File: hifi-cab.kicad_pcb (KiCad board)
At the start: 2 copper layers, 25 parts, among them J1 FAN 1, J10 BUTTON, J11 RS-232, J12 5V ENABLE, J13 PWR IN, J2 FAN VOLTAGE, J3 FAN 1, J7 IR REMOTE, J8 DS18B20, J9 DS18B20, Q1 AO3400A, Q2 AO3400A, U1 esp32-wemos-d1-mini, U2 TSR1-2433E

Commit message: Update hifi-cab.kicad_pcb
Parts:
- added REF**: MountingHole_2.5mm_Pad_TopOnly, MountingHole:MountingHole_2.5mm_Pad_TopOnly, F.Cu at (44.7, 151.6)
- moved R11 106.8 mm to (70.0, 145.0)
- moved J10 103.6 mm to (66.5, 151.4)
- moved J11 98.2 mm to (52.3, 151.5)
- moved U1 45.0 mm to (104.3, 134.8), turned to 0 degrees
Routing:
- net +3.3V: track 2.45 -> 9.19 mm
- net BTN_1: track 0.00 -> 6.48 mm

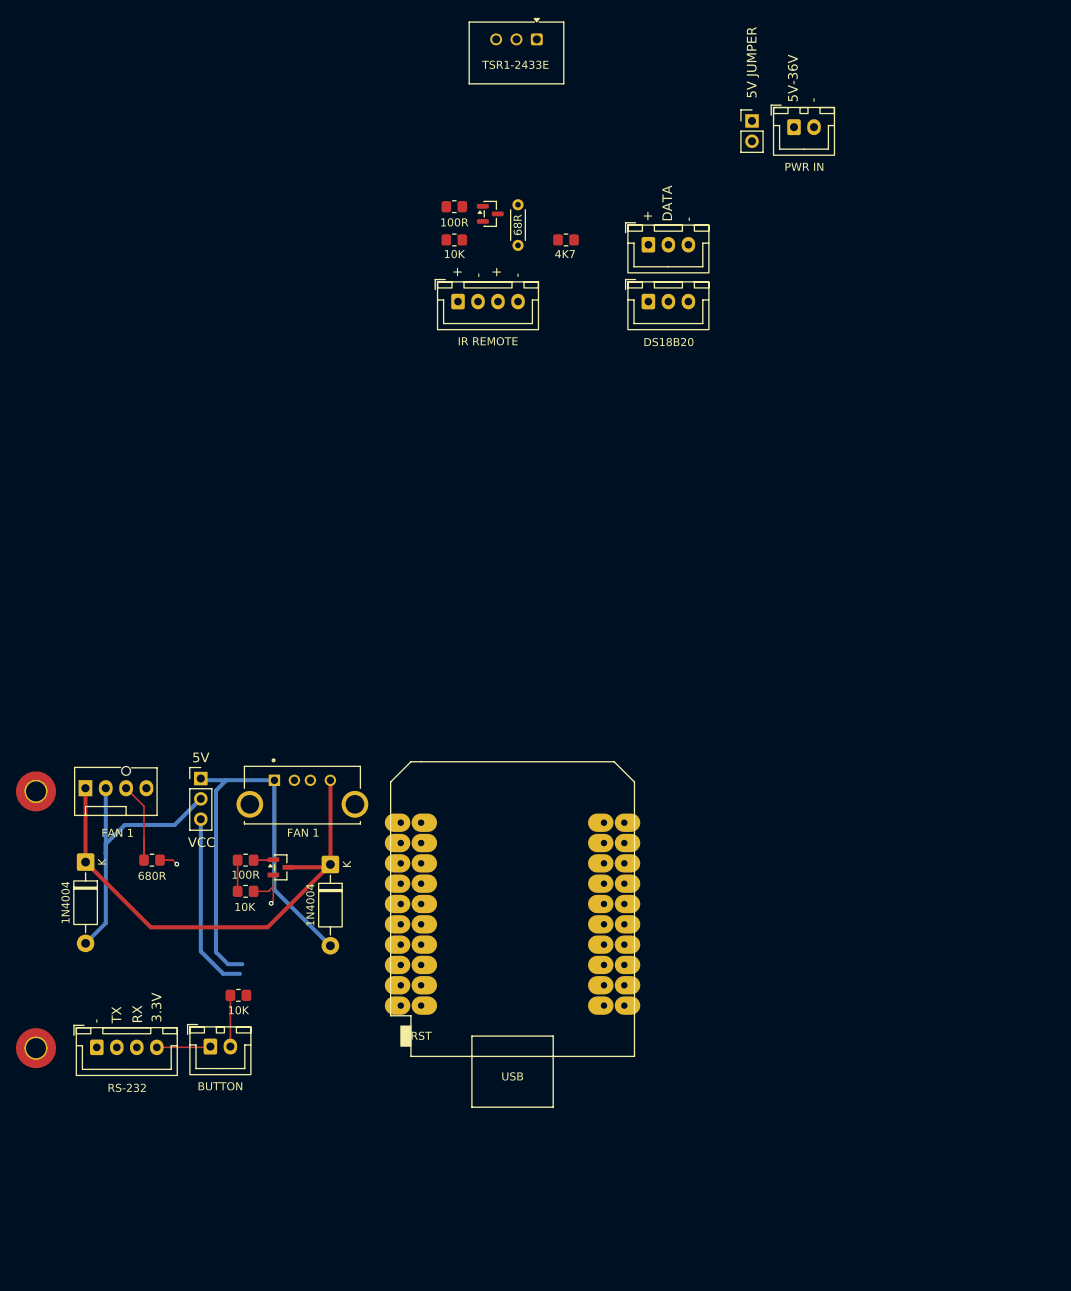
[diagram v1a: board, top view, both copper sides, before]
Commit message: Simplify, return to 5V only.
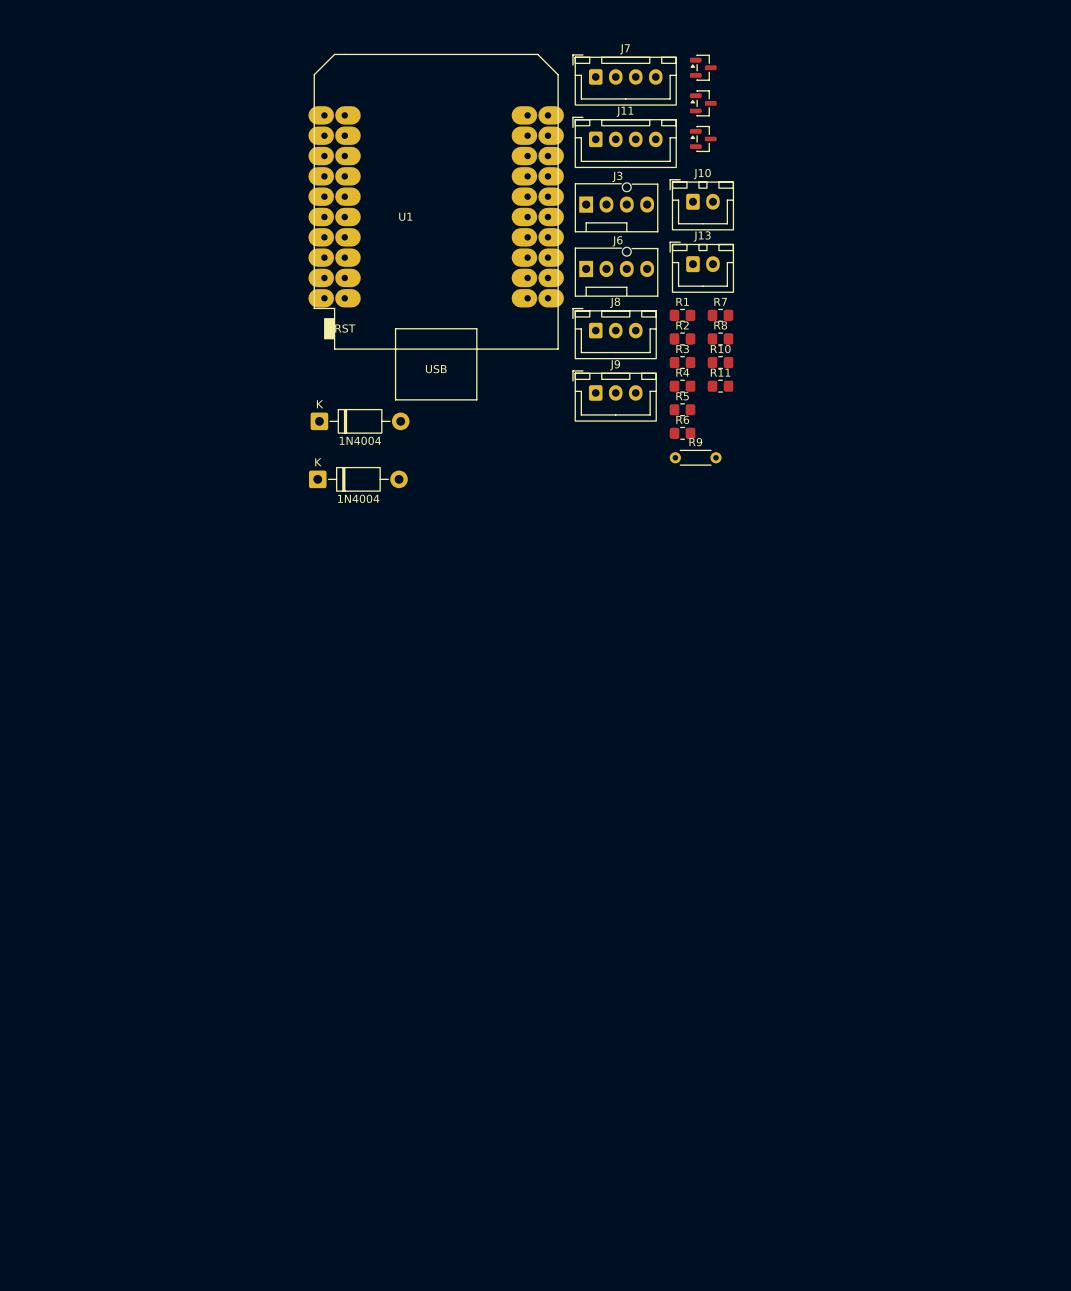
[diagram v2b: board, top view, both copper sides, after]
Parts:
- removed D1: 1N4004, Diode_THT:D_DO-41_SOD81_P10.16mm_Horizontal
- removed J1: FAN 1, USB_A1VSB6:ONSHORE_USB-A1VSB6
- removed J12: 5V ENABLE, Connector_PinHeader_2.54mm:PinHeader_1x02_P2.54mm_Vertical
- removed J2: FAN VOLTAGE, Connector_PinHeader_2.54mm:PinHeader_1x03_P2.54mm_Vertical
- removed REF** (x2): MountingHole_2.5mm_Pad_TopOnly, MountingHole:MountingHole_2.5mm_Pad_TopOnly
- removed U2: TSR1-2433E, Converter_DCDC:Converter_DCDC_TRACO_TSR1-xxxxE_THT
- added D4: 1N4004, Diode_THT:D_DO-41_SOD81_P10.16mm_Horizontal, F.Cu at (79.9, 80.5)
- added J6: FAN 2, Connector:FanPinHeader_1x04_P2.54mm_Vertical, F.Cu at (113.5, 54.2)
- added Q3: AO3400A, Package_TO_SOT_SMD:SOT-23, F.Cu at (128.1, 38.0)
- added R4: 100R, Resistor_SMD:R_0805_2012Metric_Pad1.20x1.40mm_HandSolder, F.Cu at (125.5, 68.8)
- added R5: 10K, Resistor_SMD:R_0805_2012Metric_Pad1.20x1.40mm_HandSolder, F.Cu at (125.5, 71.8)
- added R6: 680R, Resistor_SMD:R_0805_2012Metric_Pad1.20x1.40mm_HandSolder, F.Cu at (125.5, 74.8)
- moved J11 129.5 mm to (114.7, 38.0)
- moved J10 121.6 mm to (126.8, 45.8)
- moved Q1 113.0 mm to (128.1, 29.1)
- moved R11 97.1 mm to (130.3, 68.8)
- moved J3 96.1 mm to (113.5, 46.1)
- moved R3 90.9 mm to (125.5, 65.9)
- moved U1 88.9 mm to (94.7, 46.4)
- moved R2 88.0 mm to (125.5, 63.0)
- moved R1 87.3 mm to (125.5, 60.0)
- moved D2 62.4 mm to (80.1, 73.2), turned to 0 degrees
- moved R7 35.9 mm to (130.3, 60.0)
- moved R8 35.5 mm to (130.3, 63.0)
- moved R9 33.0 mm to (124.6, 77.8), turned to 0 degrees
- moved J7 32.9 mm to (114.7, 30.2)
- moved Q2 30.0 mm to (128.1, 33.5)
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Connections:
- J13 pad 1: VCC -> +5V
- U1 pad 35: unconnected-(U1-VCC_(USB)-Pad35) -> +5V
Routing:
- net FAN1: track 62.4 -> 0.00 mm
- net +5V: track 59.5 -> 0.00 mm
- net Net-(D2-A): track 35.9 -> 0.00 mm
- net VCC: track 22.6 -> 0.00 mm
- net TACH1: track 11.9 -> 0.00 mm
- net +3.3V: track 9.19 -> 0.00 mm, vias 1 -> 0
- net BTN_1: track 6.48 -> 0.00 mm
- net GND: track 6.37 -> 0.00 mm, vias 1 -> 0
- net FAN1_C: track 3.90 -> 0.00 mm
- net Net-(Q1-G): track 2.48 -> 0.00 mm
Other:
- board text removed: "+"
- board text removed: "-"
- board text removed: "3.3V"
- board text removed: "5V"
- board text removed: "5V JUMPER"
- board text removed: "5V-36V"
- board text removed: "DATA"
- board text removed: "RX"
- board text removed: "TX"
- board text removed: "VCC"

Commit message: Add cap
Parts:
- added C1: 400uF, Capacitor_THT:CP_Radial_D5.0mm_P2.50mm, F.Cu at (123.3, 59.2)
- moved Q1 80.3 mm to (110.7, 107.5), turned to 90 degrees
- moved Q3 69.6 mm to (125.7, 107.5), turned to 90 degrees
- moved R2 54.1 mm to (110.7, 115.0), turned to 180 degrees
- moved R1 53.5 mm to (110.7, 111.4), turned to 180 degrees
- moved J3 49.3 mm to (104.7, 94.7)
- moved R4 49.1 mm to (127.1, 118.0)
- moved R5 49.1 mm to (127.1, 120.9)
- moved D4 45.5 mm to (119.6, 102.7), turned to -90 degrees
- moved R9 43.6 mm to (136.6, 35.9)
- moved J6 41.0 mm to (119.6, 94.7)
- moved R3 39.3 mm to (110.8, 102.3)
- moved D2 38.4 mm to (104.7, 102.7), turned to -90 degrees
- moved R11 29.4 mm to (150.0, 47.1)
- moved J8 28.9 mm to (143.4, 65.0)
- moved J9 28.8 mm to (143.4, 71.9)
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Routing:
- net Net-(D4-A): track 0.00 -> 19.2 mm
- net Net-(D2-A): track 0.00 -> 19.2 mm
- net FAN1: track 0.00 -> 15.8 mm
- net FAN2: track 0.00 -> 15.7 mm
- net TACH1: track 0.00 -> 7.67 mm
- net TACH2: track 0.00 -> 7.62 mm
- net FAN1_C: track 0.00 -> 3.60 mm
- net Net-(Q1-G): track 0.00 -> 3.00 mm

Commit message: Update hifi-cab.kicad_pcb
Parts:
- moved R4 6.70 mm to (125.7, 111.4), turned to 180 degrees
- moved R5 6.06 mm to (125.7, 115.0), turned to 180 degrees
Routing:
- net GND: track 0.00 -> 9.89 mm, vias 0 -> 4
- net FAN2_C: track 0.00 -> 3.60 mm
- net Net-(Q3-G): track 0.00 -> 3.02 mm
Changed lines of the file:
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@@
 	(footprint "Resistor_SMD:R_0805_2012Metric_Pad1.20x1.40mm_HandSolder"
 		(layer "F.Cu")
-		(at 127.1 120.9)
+		(at 125.7 115 180)
 		(descr "Resistor SMD 0805 (2012 Metric), square (rectangular) end terminal, IPC-7351 nominal with elongated pad for handsoldering. (Body size source: IPC-SM-782 page 72, https://www.pcb-3d.com/wordpress/wp-content/uploads/ipc-sm-782a_amendment_1_and_2.pdf), generated with kicad-footprint-generator")
 		(tags "resistor handsolder")
@@
 		)
 		(property "Value" "10K"
-			(at 0 1.65 0)
+			(at 0 -1.8 0)
 			(layer "F.SilkS")
 			(effects
@@
 		(attr smd)
 		(fp_line
-			(start -0.227064 -0.735)
-			(end 0.227064 -0.735)
+			(start -0.227064 0.735)
+			(end 0.227064 0.735)
 			(stroke
 				(width 0.12)
@@
 		)
 		(fp_line
-			(start -0.227064 0.735)
-			(end 0.227064 0.735)
+			(start -0.227064 -0.735)
+			(end 0.227064 -0.735)
 			(stroke
 				(width 0.12)
@@
 		)
 		(pad "1" smd roundrect
-			(at -1 0)
+			(at -1 0 180)
 			(size 1.2 1.4)
 			(layers "F.Cu" "F.Mask" "F.Paste")
@@
 		)
 		(pad "2" smd roundrect
-			(at 1 0)
+			(at 1 0 180)
 			(size 1.2 1.4)
 			(layers "F.Cu" "F.Mask" "F.Paste")
@@
 	(footprint "Resistor_SMD:R_0805_2012Metric_Pad1.20x1.40mm_HandSolder"
 		(layer "F.Cu")
-		(at 127.1 117.95)
+		(at 125.7 111.4 180)
 		(descr "Resistor SMD 0805 (2012 Metric), square (rectangular) end terminal, IPC-7351 nominal with elongated pad for handsoldering. (Body size source: IPC-SM-782 page 72, https://www.pcb-3d.com/wordpress/wp-content/uploads/ipc-sm-782a_amendment_1_and_2.pdf), generated with kicad-footprint-generator")
 		(tags "resistor handsolder")
@@
 		)
 		(property "Value" "100R"
-			(at 0 1.65 0)
+			(at 0 -1.8 0)
 			(layer "F.SilkS")
 			(effects
@@
 		(attr smd)
 		(fp_line
-			(start -0.227064 -0.735)
-			(end 0.227064 -0.735)
+			(start -0.227064 0.735)
+			(end 0.227064 0.735)
 			(stroke
 				(width 0.12)
@@
 		)
 		(fp_line
-			(start -0.227064 0.735)
-			(end 0.227064 0.735)
+			(start -0.227064 -0.735)
+			(end 0.227064 -0.735)
 			(stroke
 				(width 0.12)
@@
 		)
 		(pad "1" smd roundrect
-			(at -1 0)
+			(at -1 0 180)
 			(size 1.2 1.4)
 			(layers "F.Cu" "F.Mask" "F.Paste")
@@
 		)
 		(pad "2" smd roundrect
-			(at 1 0)
+			(at 1 0 180)
 			(size 1.2 1.4)
 			(layers "F.Cu" "F.Mask" "F.Paste")
@@
 	)
 	(segment
+		(start 124.65 115.05)
+		(end 123.75 114.15)
+		(width 0.2)
+		(layer "F.Cu")
+		(net 11)
+	)
+	(segment
+		(start 111.6 108.4)
+		(end 112.5 109.3)
+		(width 0.2)
+		(layer "F.Cu")
+		(net 11)
+	)
+	(segment
+		(start 126.65 108.35)
+		(end 127.55 109.25)
+		(width 0.2)
+		(layer "F.Cu")
+		(net 11)
+	)
+	(segment
+		(start 127.55 109.25)
+		(end 128.75 109.25)
+		(width 0.2)
+		(layer "F.Cu")
+		(net 11)
+	)
+	(segment
+		(start 123.75 114.15)
+		(end 122.55 114.15)
+		(width 0.2)
+		(layer "F.Cu")
+		(net 11)
+	)
+	(segment
+		(start 109.65 115.15)
+		(end 108.75 114.25)
+		(width 0.2)
+		(layer "F.Cu")
+		(net 11)
+	)
+	(segment
+		(start 108.75 114.25)
+		(end 107.55 114.25)
+		(width 0.2)
+		(layer "F.Cu")
+		(net 11)
+	)
+	(segment
+		(start 112.5 109.3)
+		(end 113.7 109.3)
+		(width 0.2)
+		(layer "F.Cu")
+		(net 11)
+	)
+	(via
+		(at 128.75 109.25)
+		(size 0.6)
+		(drill 0.3)
+		(layers "F.Cu" "B.Cu")
+		(net 11)
+	)
+	(via
+		(at 107.55 114.25)
+		(size 0.6)
+		(drill 0.3)
+		(layers "F.Cu" "B.Cu")
+		(net 11)
+	)
+	(via
+		(at 122.55 114.15)
+		(size 0.6)
+		(drill 0.3)
+		(layers "F.Cu" "B.Cu")
+		(net 11)
+	)
+	(via
+		(at 113.7 109.3)
+		(size 0.6)
+		(drill 0.3)
+		(layers "F.Cu" "B.Cu")
+		(net 11)
+	)
+	(segment
 		(start 109.7 108.4)
 		(end 109.7 111.4)
@@
 	)
 	(segment
+		(start 126.7 111.4)
+		(end 126.7 115)
+		(width 0.2)
+		(layer "F.Cu")
+		(net 20)
+	)
+	(segment
 		(start 125.7 106.525)
 		(end 121.895 102.72)
@@
 		(net 46)
 	)
+	(segment
+		(start 124.75 111.35)
+		(end 124.7 111.4)
+		(width 0.2)
+		(layer "F.Cu")
+		(net 47)
+	)
+	(segment
+		(start 124.75 108.4)
+		(end 124.75 111.35)
+		(width 0.2)
+		(layer "F.Cu")
+		(net 47)
+	)
 	(embedded_fonts no)

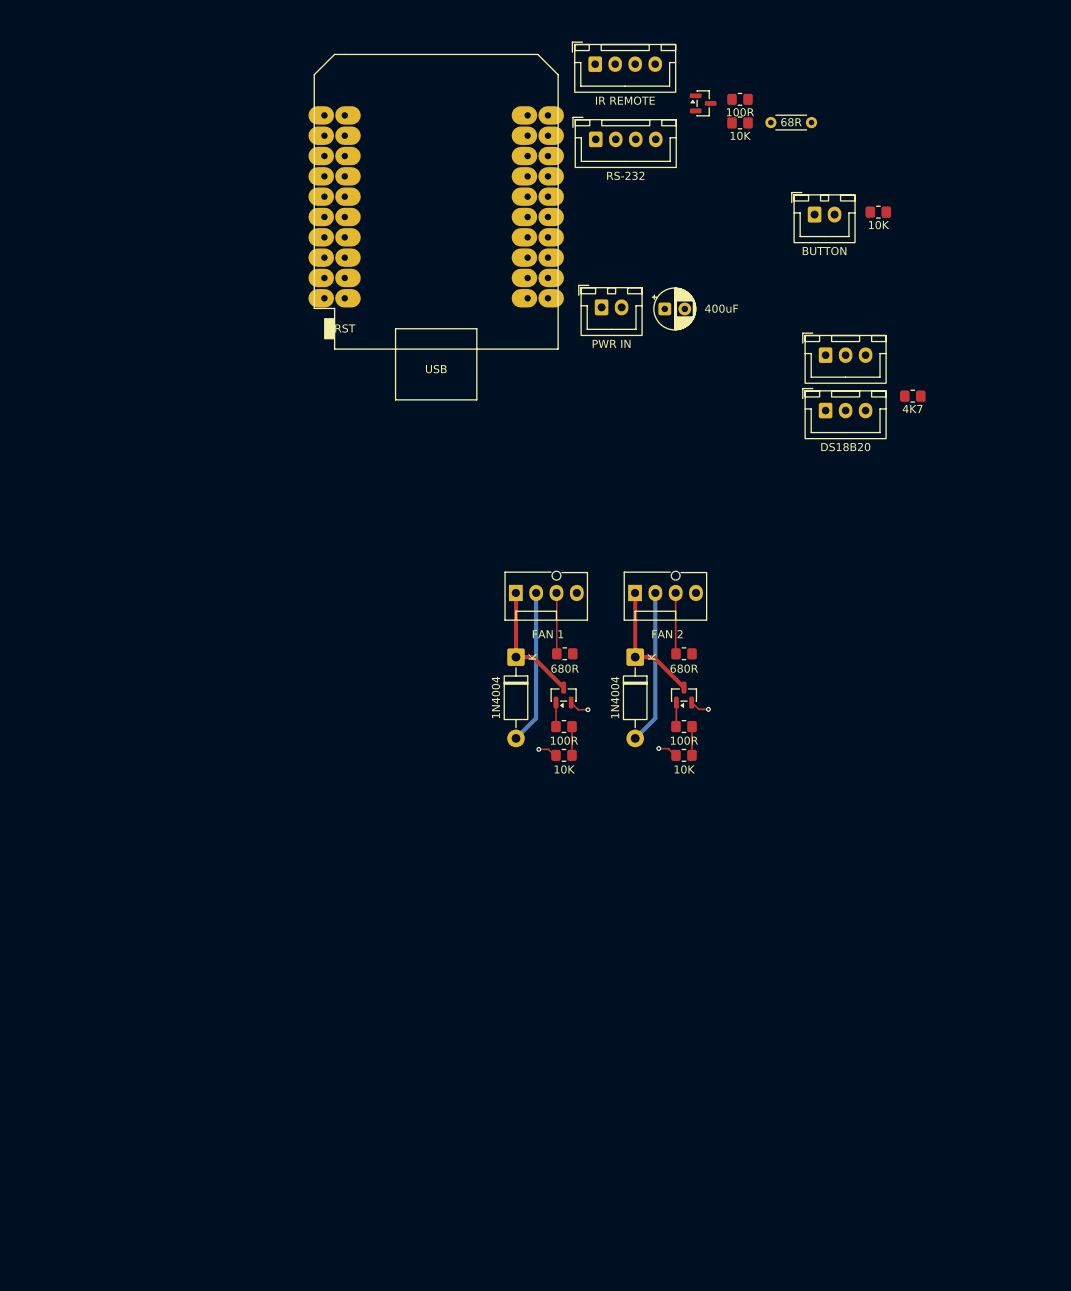
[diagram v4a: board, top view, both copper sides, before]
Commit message: Fix power on schematic
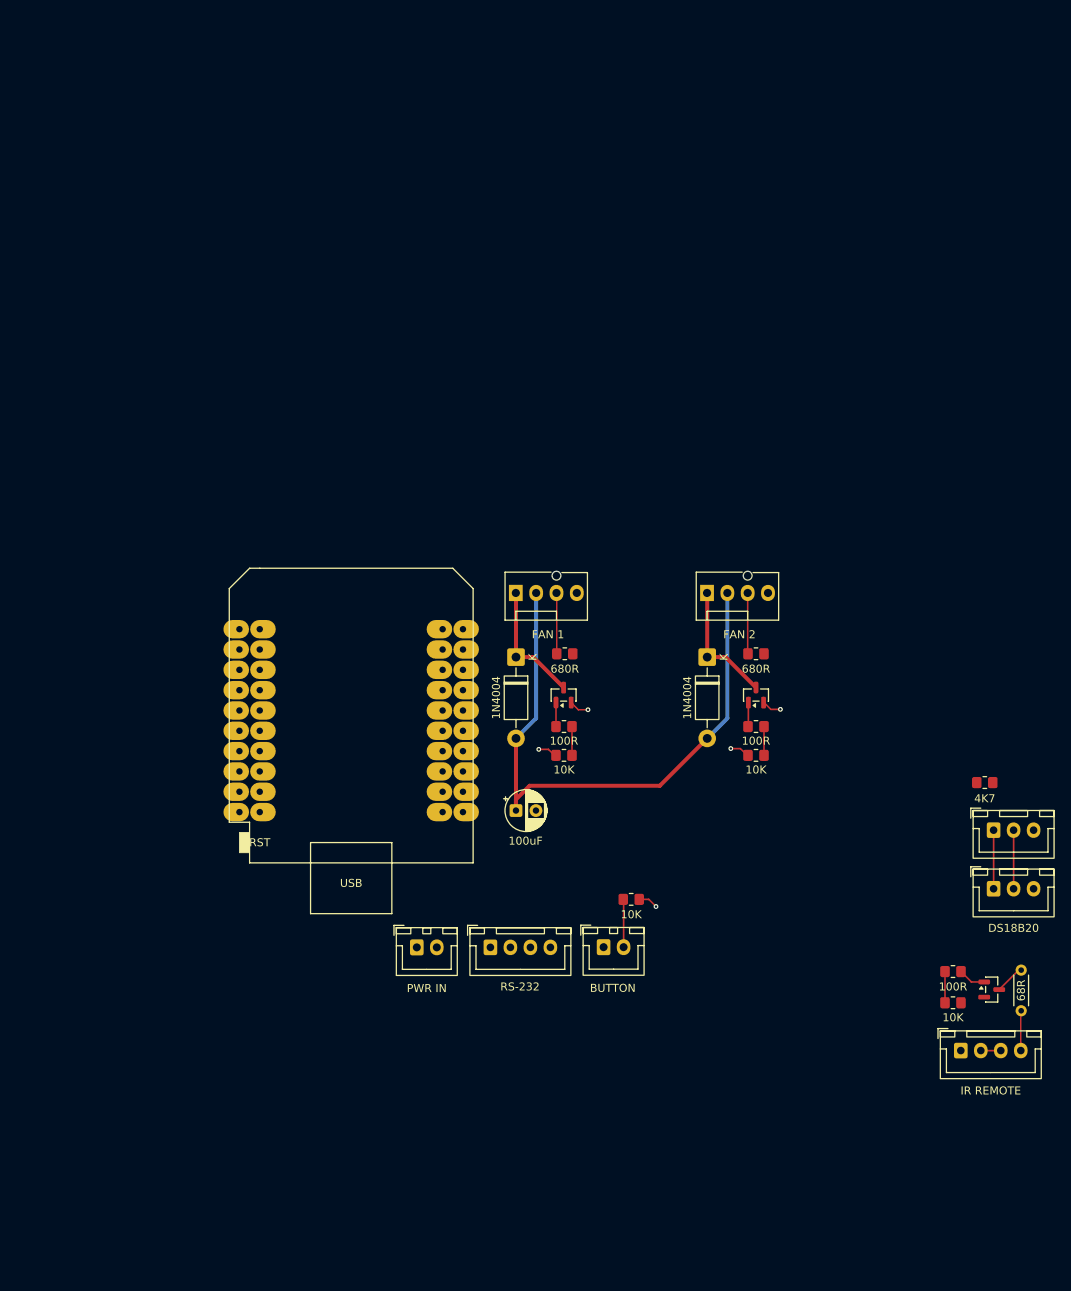
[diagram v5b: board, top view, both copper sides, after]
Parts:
- C1: value 400uF -> 100uF
- moved J7 131.5 mm to (160.3, 151.9)
- moved Q2 116.5 mm to (164.2, 144.3)
- moved R9 115.3 mm to (167.8, 146.9), turned to 90 degrees
- moved R8 113.2 mm to (159.3, 145.9)
- moved R7 112.2 mm to (159.3, 142.0)
- moved J11 101.9 mm to (101.5, 139.0)
- moved J10 95.3 mm to (115.7, 139.0)
- moved R11 91.3 mm to (119.1, 133.0)
- moved J13 83.3 mm to (92.3, 139.0)
- moved C1 65.4 mm to (104.7, 121.9)
- moved U1 65.1 mm to (84.1, 110.7)
- moved J9 63.4 mm to (164.4, 131.7)
- moved J8 63.0 mm to (164.4, 124.3)
- moved R10 49.1 mm to (163.3, 118.4), turned to 180 degrees
- moved J6 9.00 mm to (128.6, 94.7)
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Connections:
- D2 pad 2: Net-(D2-A) -> +5V
- D4 pad 2: Net-(D4-A) -> +5V
- J3 pad 2: Net-(D2-A) -> +5V
- J6 pad 2: Net-(D4-A) -> +5V
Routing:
- net +5V: track 0.00 -> 75.9 mm
- net Net-(D4-A): track 19.2 -> 0.00 mm
- net Net-(D2-A): track 19.2 -> 0.00 mm
- net DS18B20: track 0.00 -> 7.33 mm
- net +3.3V: track 0.00 -> 7.33 mm
- net BTN_1: track 0.00 -> 6.00 mm
- net Net-(J7-Pin_4): track 0.00 -> 5.00 mm
- net IR_C: track 0.00 -> 3.90 mm
- net IR_1: track 0.00 -> 3.76 mm
- net Net-(Q2-G): track 0.00 -> 3.44 mm
- net Net-(J7-Pin_2): track 0.00 -> 2.50 mm
- net GND: track 9.89 -> 12.4 mm, vias 4 -> 5

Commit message: Explore layout.
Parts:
- added ?: , , F.Cu at (131.3, 128.4)
- added U2: TSR0.5-2433, Converter_DCDC:Converter_DCDC_TRACO_TSR0.5-24xx_TSR0.5-24xxx_THT, F.Cu at (107.5, 128.1)
- moved J8 45.5 mm to (119.5, 131.5)
- moved J9 45.5 mm to (119.5, 138.8)
- moved R10 45.5 mm to (118.4, 125.5)
- moved C1 32.9 mm to (73.5, 132.3), turned to 180 degrees
- moved Q2 32.1 mm to (135.1, 130.7)
- moved R7 32.1 mm to (130.3, 128.4)
- moved R8 32.1 mm to (130.3, 132.3)
- moved R9 32.1 mm to (138.8, 133.3)
- moved J7 31.8 mm to (131.3, 138.8)
- moved J13 21.2 mm to (71.1, 139.0)
- moved J11 20.9 mm to (80.6, 139.0)
- moved J10 5.95 mm to (109.7, 138.9)
- moved R11 5.95 mm to (113.2, 132.9)
- moved J6 5.40 mm to (123.2, 94.7)
- moved D4 5.40 mm to (123.2, 102.7)
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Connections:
- C1 pad 1: +5V -> VCC
- D2 pad 2: +5V -> VCC
- D4 pad 2: +5V -> VCC
- J13 pad 1: +5V -> GND
- J13 pad 2: GND -> VCC
- J3 pad 2: +5V -> VCC
- J6 pad 2: +5V -> VCC
- U1 pad 35: +5V -> unconnected-(U1-VCC_(USB)-Pad35)
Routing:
- net VCC: track 0.00 -> 124.0 mm
- net +5V: track 75.9 -> 0.00 mm
- net +3.3V: track 7.33 -> 21.6 mm
- net Net-(J7-Pin_4): track 5.00 -> 0.07 mm
- net Net-(J7-Pin_2): track 2.50 -> 0.00 mm
